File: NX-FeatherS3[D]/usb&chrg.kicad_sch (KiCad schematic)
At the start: 24 parts, among them J1 USB_C_Receptacle_USB2.0_14P, J4 Conn_01x02_Pin, Q1 Q_PMOS, U2 NCP167BMX330TBG, U8 BQ25170DSGR

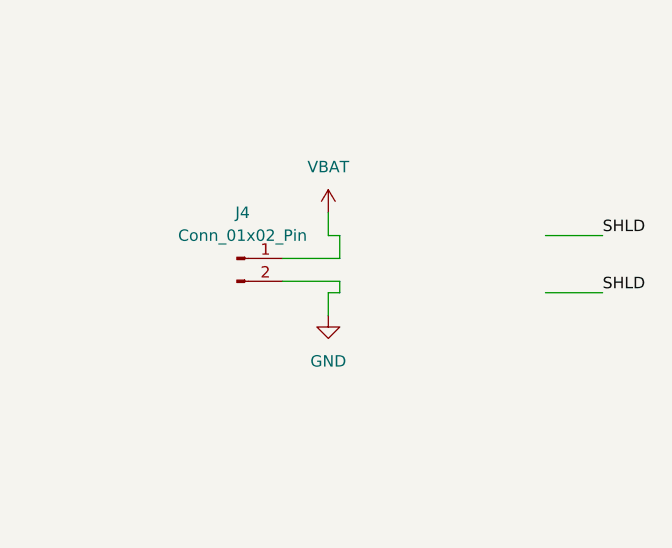
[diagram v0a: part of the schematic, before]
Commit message: Added v1p0, updated Version
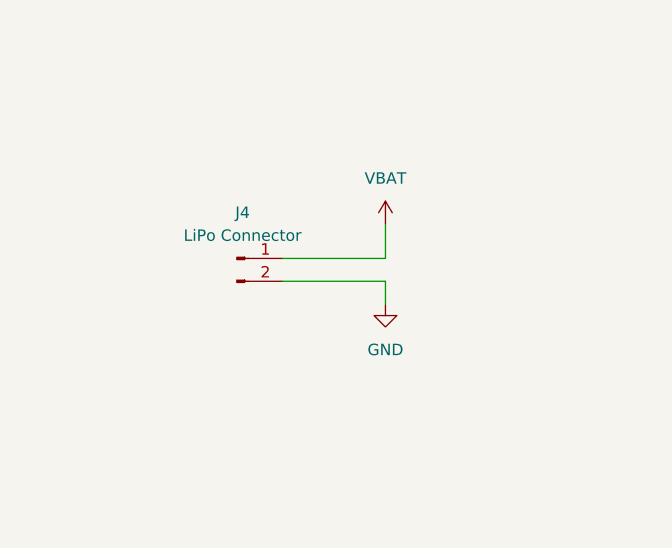
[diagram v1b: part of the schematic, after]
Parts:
- J4: value Conn_01x02_Pin -> LiPo Connector
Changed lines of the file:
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@@
 	(wire
 		(pts
-			(xy 220.98 48.26) (xy 220.98 45.72)
+			(xy 227.33 46.99) (xy 227.33 44.45)
 		)
 		(stroke
@@
 	(wire
 		(pts
-			(xy 222.25 44.45) (xy 215.9 44.45)
+			(xy 215.9 44.45) (xy 227.33 44.45)
 		)
 		(stroke
@@
 	(wire
 		(pts
-			(xy 220.98 39.37) (xy 222.25 39.37)
-		)
-		(stroke
-			(width 0)
-			(type default)
-		)
-	)
-	(wire
-		(pts
 			(xy 185.42 119.38) (xy 185.42 120.65)
 		)
@@
 	(wire
 		(pts
-			(xy 222.25 45.72) (xy 222.25 44.45)
-		)
-		(stroke
-			(width 0)
-			(type default)
-		)
-	)
-	(wire
-		(pts
 			(xy 181.61 101.6) (xy 175.26 101.6)
 		)
@@
 	(wire
 		(pts
-			(xy 245.11 45.72) (xy 251.46 45.72)
-		)
-		(stroke
-			(width 0)
-			(type default)
-		)
-	)
-	(wire
-		(pts
 			(xy 62.23 31.75) (xy 62.23 49.53)
 		)
@@
 	(wire
 		(pts
-			(xy 222.25 41.91) (xy 215.9 41.91)
+			(xy 215.9 41.91) (xy 227.33 41.91)
 		)
 		(stroke
@@
 	(wire
 		(pts
-			(xy 220.98 36.83) (xy 220.98 39.37)
+			(xy 227.33 38.1) (xy 227.33 41.91)
 		)
 		(stroke
@@
 	(wire
 		(pts
-			(xy 222.25 39.37) (xy 222.25 41.91)
-		)
-		(stroke
-			(width 0)
-			(type default)
-		)
-	)
-	(wire
-		(pts
 			(xy 137.16 132.08) (xy 129.54 132.08)
 		)
@@
 	(wire
 		(pts
-			(xy 220.98 45.72) (xy 222.25 45.72)
-		)
-		(stroke
-			(width 0)
-			(type default)
-		)
-	)
-	(wire
-		(pts
 			(xy 176.53 129.54) (xy 191.77 129.54)
 		)
@@
 		(pts
 			(xy 175.26 99.06) (xy 175.26 101.6)
-		)
-		(stroke
-			(width 0)
-			(type default)
-		)
-	)
-	(wire
-		(pts
-			(xy 245.11 39.37) (xy 251.46 39.37)
 		)
 		(stroke
@@
 		)
 	)
-	(label "SHLD"
-		(at 251.46 45.72 0)
-		(effects
-			(font
-				(size 1.27 1.27)
-			)
-			(justify left bottom)
-		)
-	)
 	(label "USB_P"
 		(at 45.72 124.46 180)
@@
 	(label "CC2"
 		(at 66.04 31.75 0)
-		(effects
-			(font
-				(size 1.27 1.27)
-			)
-			(justify left bottom)
-		)
-	)
-	(label "SHLD"
-		(at 251.46 39.37 0)
 		(effects
 			(font
@@
 	(symbol
 		(lib_id "power:GND")
-		(at 220.98 48.26 0)
+		(at 227.33 46.99 0)
 		(unit 1)
 		(exclude_from_sim no)
@@
 		(fields_autoplaced yes)
 		(property "Reference" "#PWR06"
-			(at 220.98 54.61 0)
+			(at 227.33 53.34 0)
 			(effects
 				(font
@@
 		)
 		(property "Value" "GND"
-			(at 220.98 53.34 0)
+			(at 227.33 52.07 0)
 			(effects
 				(font
@@
 		)
 		(property "Footprint" ""
-			(at 220.98 48.26 0)
+			(at 227.33 46.99 0)
 			(effects
 				(font
@@
 		)
 		(property "Datasheet" ""
-			(at 220.98 48.26 0)
+			(at 227.33 46.99 0)
 			(effects
 				(font
@@
 		)
 		(property "Description" "Power symbol creates a global label with name \"GND\" , ground"
-			(at 220.98 48.26 0)
+			(at 227.33 46.99 0)
 			(effects
 				(font
@@
 	(symbol
 		(lib_id "power:VBUS")
-		(at 220.98 36.83 0)
+		(at 227.33 38.1 0)
 		(unit 1)
 		(exclude_from_sim no)
@@
 		(fields_autoplaced yes)
 		(property "Reference" "#PWR013"
-			(at 220.98 40.64 0)
+			(at 227.33 41.91 0)
 			(effects
 				(font
@@
 		)
 		(property "Value" "VBAT"
-			(at 220.98 31.75 0)
+			(at 227.33 33.02 0)
 			(effects
 				(font
@@
 		)
 		(property "Footprint" ""
-			(at 220.98 36.83 0)
+			(at 227.33 38.1 0)
 			(effects
 				(font
@@
 		)
 		(property "Datasheet" ""
-			(at 220.98 36.83 0)
+			(at 227.33 38.1 0)
 			(effects
 				(font
@@
 		)
 		(property "Description" "Power symbol creates a global label with name \"VBUS\""
-			(at 220.98 36.83 0)
+			(at 227.33 38.1 0)
 			(effects
 				(font
@@
 			)
 		)
-		(property "Value" "Conn_01x02_Pin"
+		(property "Value" "LiPo Connector"
 			(at 211.455 39.37 0)
 			(effects
